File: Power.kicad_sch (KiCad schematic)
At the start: 37 parts, among them J2 Conn_01x02, J3 ZX62-B-5PA_33_, U1 MPM3610GQV-Z, U2 CH340E, U4 TPS2117DRLR, U5 BD33IC0WEFJ-E2

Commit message: 回路図（ひとまず完成）
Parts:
- R1: footprint (none) -> KIR03EZPF1003:RES_R0603_ROM-L
- R26, R28, R30, R32: footprint (none) -> KIR03EZPF1003:RES_R0603_ROM-M
- R27: value 19K1_0.1% -> 19.1K_0.1%
- TP1, TP2, TP3, TP4: footprint (none) -> TestPoint:TestPoint_Pad_3.0x3.0mm
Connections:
- net VIN_5V: now also R28.2; no longer R28.1
- net at R27.1, U1.1 (FB): now also R28.1; no longer R28.2
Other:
- note removed: "ROHM"
- note removed: "実際にはBD33IC0JEFJ-E2を指定する？"
- moved on the sheet: R27, R28
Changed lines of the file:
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@@
 		)
 	)
-	(text "ROHM"
-		(exclude_from_sim no)
-		(at 154.432 219.456 0)
-		(effects
-			(font
-				(size 1.27 1.27)
-			)
-		)
-	)
 	(text "バリスタ"
 		(exclude_from_sim no)
@@
 		)
 	)
-	(text "実際にはBD33IC0JEFJ-E2を指定する？\n"
-		(exclude_from_sim no)
-		(at 156.464 222.25 0)
-		(effects
-			(font
-				(size 1.27 1.27)
-			)
-		)
-	)
 	(text "5V 昇降圧回路"
 		(exclude_from_sim no)
@@
 			)
 		)
-		(property "Footprint" ""
+		(property "Footprint" "KIR03EZPF1003:RES_R0603_ROM-M"
 			(at 391.668 64.77 90)
 			(hide yes)
@@
 			)
 		)
-		(property "Footprint" ""
+		(property "Footprint" "KIR03EZPF1003:RES_R0603_ROM-M"
 			(at 315.722 68.58 90)
 			(hide yes)
@@
 	(symbol
 		(lib_id "Device:R")
-		(at 144.78 140.97 180)
+		(at 144.78 140.97 0)
+		(mirror y)
 		(unit 1)
 		(body_style 1)
@@
 		(fields_autoplaced yes)
 		(property "Reference" "R28"
-			(at 142.24 142.2401 0)
+			(at 142.24 139.6999 0)
 			(show_name no)
 			(do_not_autoplace no)
@@
 		)
 		(property "Value" "100K_1%"
-			(at 142.24 139.7001 0)
+			(at 142.24 142.2399 0)
 			(show_name no)
 			(do_not_autoplace no)
@@
 			)
 		)
-		(property "Footprint" ""
+		(property "Footprint" "KIR03EZPF1003:RES_R0603_ROM-M"
 			(at 146.558 140.97 90)
 			(hide yes)
@@
 			)
 		)
-		(property "Footprint" ""
+		(property "Footprint" "KIR03EZPF1003:RES_R0603_ROM-L"
 			(at 48.26 142.748 90)
 			(hide yes)
@@
 			)
 		)
-		(property "Footprint" ""
+		(property "Footprint" "TestPoint:TestPoint_Pad_3.0x3.0mm"
 			(at 231.14 43.18 0)
 			(hide yes)
@@
 			)
 		)
-		(property "Footprint" ""
+		(property "Footprint" "TestPoint:TestPoint_Pad_3.0x3.0mm"
 			(at 274.32 55.88 0)
 			(hide yes)
@@
 			)
 		)
-		(property "Footprint" ""
+		(property "Footprint" "KIR03EZPF1003:RES_R0603_ROM-M"
 			(at 56.388 152.4 90)
 			(hide yes)
@@
 			)
 		)
-		(property "Footprint" ""
+		(property "Footprint" "TestPoint:TestPoint_Pad_3.0x3.0mm"
 			(at 391.16 76.2 0)
 			(hide yes)
@@
 	(symbol
 		(lib_id "Device:R")
-		(at 144.78 125.73 180)
+		(at 144.78 125.73 0)
+		(mirror x)
 		(unit 1)
 		(body_style 1)
@@
 		(fields_autoplaced yes)
 		(property "Reference" "R27"
-			(at 142.24 127.0001 0)
+			(at 142.24 124.4599 0)
 			(show_name no)
 			(do_not_autoplace no)
@@
 					(size 1.27 1.27)
 				)
-				(justify left)
+				(justify right)
 			)
 		)
-		(property "Value" "19K1_0.1%"
-			(at 142.24 124.4601 0)
+		(property "Value" "19.1K_0.1%"
+			(at 142.24 126.9999 0)
 			(show_name no)
 			(do_not_autoplace no)
@@
 					(size 1.27 1.27)
 				)
-				(justify left)
+				(justify right)
 			)
 		)
 		(property "Footprint" ""
-			(at 146.558 125.73 90)
+			(at 143.002 125.73 90)
 			(hide yes)
 			(show_name no)
@@
 			)
 		)
-		(property "Footprint" ""
+		(property "Footprint" "TestPoint:TestPoint_Pad_3.0x3.0mm"
 			(at 237.49 52.07 0)
 			(hide yes)

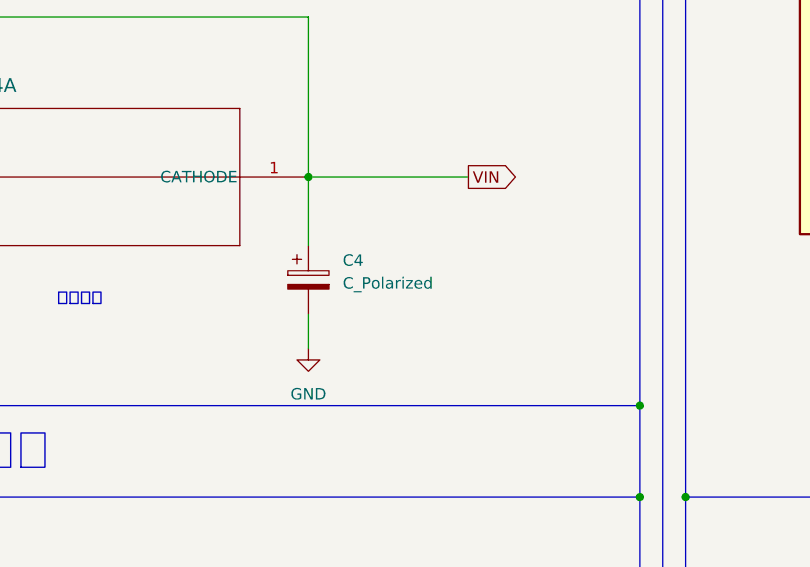
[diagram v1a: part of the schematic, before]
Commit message: 抵抗器のフットプリントを策定
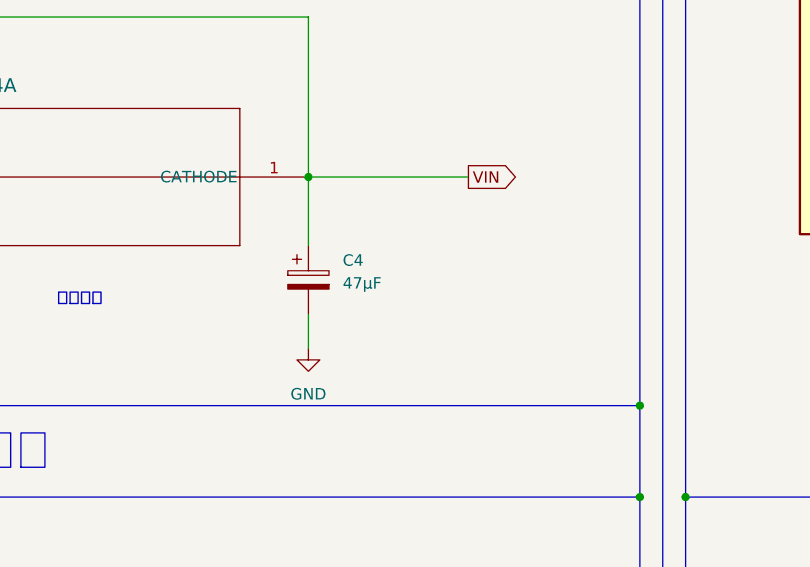
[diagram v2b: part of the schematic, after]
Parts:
- C1, C6, C7, C9: footprint (none) -> Capacitor_SMD:C_1206_3216Metric_Pad1.33x1.80mm_HandSolder
- C10, C11, C2, C5, C8: footprint (none) -> Capacitor_SMD:C_0603_1608Metric_Pad1.08x0.95mm_HandSolder
- C4: value C_Polarized -> 47µF; footprint (none) -> Capacitor_SMD:C_1206_3216Metric_Pad1.33x1.80mm_HandSolder
- R27, R29, R37: footprint (none) -> Resistor_SMD:R_0603_1608Metric_Pad0.98x0.95mm_HandSolder
- R31: footprint (none) -> Resistor_SMD:R_0805_2012Metric_Pad1.20x1.40mm_HandSolder
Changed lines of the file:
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@@
 			)
 		)
-		(property "Footprint" ""
+		(property "Footprint" "Resistor_SMD:R_0603_1608Metric_Pad0.98x0.95mm_HandSolder"
 			(at 286.512 39.37 90)
 			(hide yes)
@@
 			)
 		)
-		(property "Footprint" ""
+		(property "Footprint" "Capacitor_SMD:C_0603_1608Metric_Pad1.08x0.95mm_HandSolder"
 			(at 176.2252 254 0)
 			(hide yes)
@@
 			)
 		)
-		(property "Footprint" ""
+		(property "Footprint" "Capacitor_SMD:C_0603_1608Metric_Pad1.08x0.95mm_HandSolder"
 			(at 204.1652 160.02 0)
 			(hide yes)
@@
 			)
 		)
-		(property "Footprint" ""
+		(property "Footprint" "Capacitor_SMD:C_0603_1608Metric_Pad1.08x0.95mm_HandSolder"
 			(at 105.1052 255.27 0)
 			(hide yes)
@@
 			)
 		)
-		(property "Footprint" ""
+		(property "Footprint" "Capacitor_SMD:C_0603_1608Metric_Pad1.08x0.95mm_HandSolder"
 			(at 157.1752 137.16 0)
 			(hide yes)
@@
 			)
 		)
-		(property "Footprint" ""
+		(property "Footprint" "Capacitor_SMD:C_1206_3216Metric_Pad1.33x1.80mm_HandSolder"
 			(at 169.8752 137.16 0)
 			(hide yes)
@@
 			)
 		)
-		(property "Footprint" ""
+		(property "Footprint" "Capacitor_SMD:C_1206_3216Metric_Pad1.33x1.80mm_HandSolder"
 			(at 262.5852 43.18 0)
 			(hide yes)
@@
 			)
 		)
-		(property "Footprint" ""
+		(property "Footprint" "Capacitor_SMD:C_0603_1608Metric_Pad1.08x0.95mm_HandSolder"
 			(at 33.9852 153.67 0)
 			(hide yes)
@@
 			)
 		)
-		(property "Footprint" ""
+		(property "Footprint" "Resistor_SMD:R_0603_1608Metric_Pad0.98x0.95mm_HandSolder"
 			(at 196.342 247.65 90)
 			(hide yes)
@@
 			)
 		)
-		(property "Footprint" ""
+		(property "Footprint" "Capacitor_SMD:C_1206_3216Metric_Pad1.33x1.80mm_HandSolder"
 			(at 276.5552 43.18 0)
 			(hide yes)
@@
 			)
 		)
-		(property "Value" "C_Polarized"
+		(property "Value" "47µF"
 			(at 153.67 79.1209 0)
 			(show_name no)
@@
 			)
 		)
-		(property "Footprint" ""
+		(property "Footprint" "Capacitor_SMD:C_1206_3216Metric_Pad1.33x1.80mm_HandSolder"
 			(at 150.8252 82.55 0)
 			(hide yes)
@@
 			)
 		)
-		(property "Footprint" ""
+		(property "Footprint" "Resistor_SMD:R_0805_2012Metric_Pad1.20x1.40mm_HandSolder"
 			(at 315.722 80.01 90)
 			(hide yes)
@@
 			)
 		)
-		(property "Footprint" ""
+		(property "Footprint" "Capacitor_SMD:C_1206_3216Metric_Pad1.33x1.80mm_HandSolder"
 			(at 27.6352 166.37 0)
 			(hide yes)
@@
 			)
 		)
-		(property "Footprint" ""
+		(property "Footprint" "Resistor_SMD:R_0603_1608Metric_Pad0.98x0.95mm_HandSolder"
 			(at 143.002 125.73 90)
 			(hide yes)
